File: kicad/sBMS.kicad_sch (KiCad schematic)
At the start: 6 parts, among them J1 SWD, J2 CAN, J3 Conn_01x01_Socket, J4 Conn_01x01_Socket, J5 Conn_01x01_Socket, J6 Conn_01x01_Socket

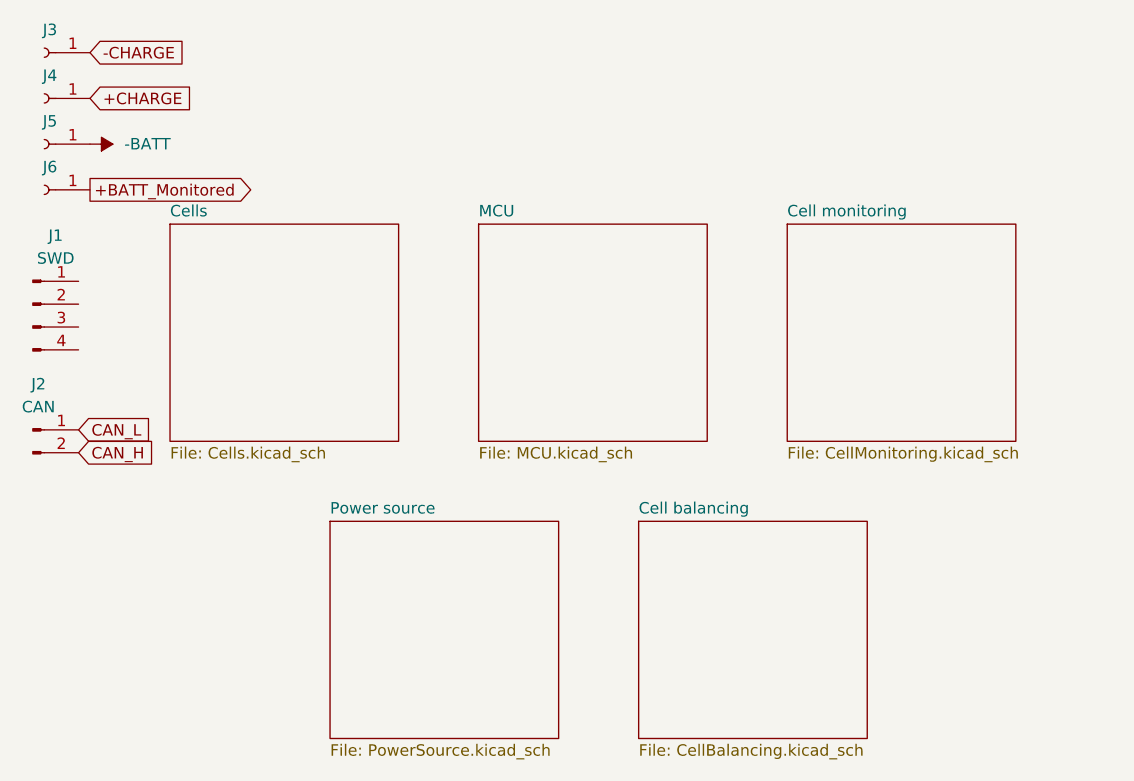
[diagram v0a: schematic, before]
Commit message: fixed cell layout, started making balancing circuitry
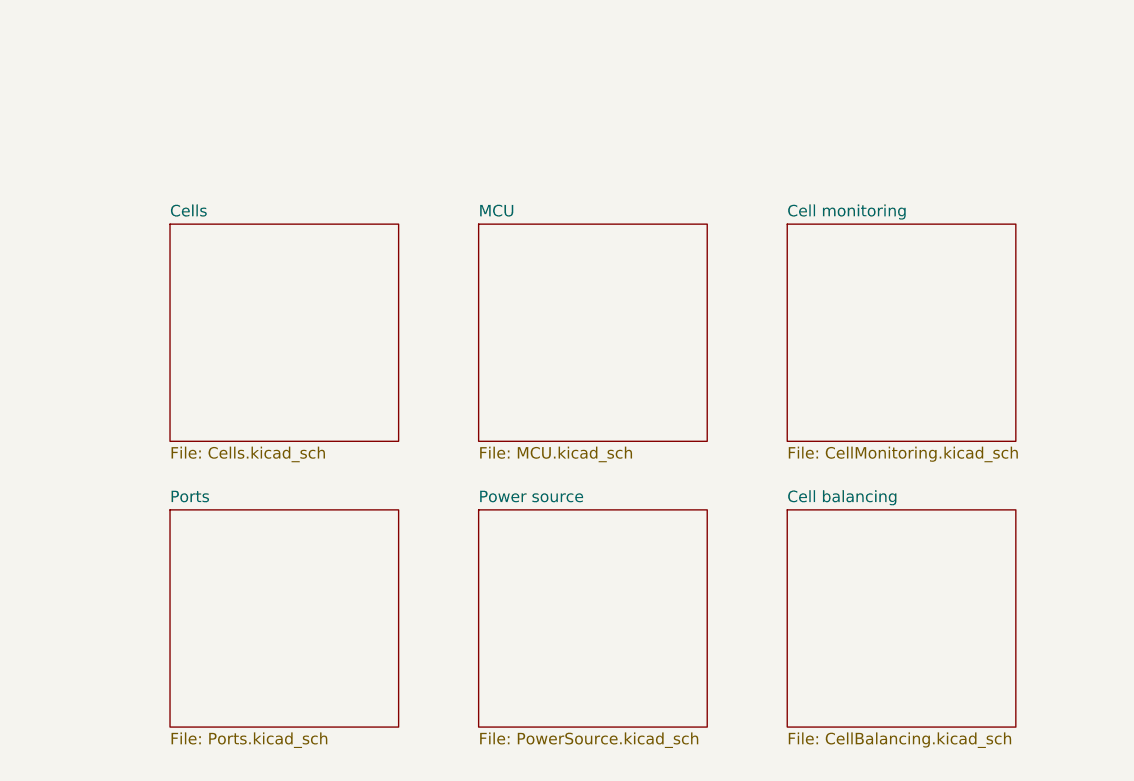
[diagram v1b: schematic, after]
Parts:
- removed J1: SWD, symbol Connector:Conn_01x04_Male
- removed J2: CAN, symbol Connector:Conn_01x02_Male
- removed J3, J4, J5, J6: Conn_01x01_Socket, symbol Connector:Conn_01x01_Socket
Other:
- added sheet Ports (Ports.kicad_sch)
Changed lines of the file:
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@@
     (date "2023-08-20")
-  )
-  (global_label "+BATT_Monitored" (shape output) (at 22.86 34.29 0) (fields_autoplaced)
-    (effects (font (size 1.27 1.27)) (justify left))
-    (property "Intersheetrefs" "${INTERSHEET_REFS}" (at 41.9317 34.29 0)
-      (effects (font (size 1.27 1.27)) (justify left) hide)
-    )
-  )
-  (global_label "CAN_L" (shape input) (at 21.59 60.96 0) (fields_autoplaced)
-    (effects (font (size 1.27 1.27)) (justify left))
-    (property "Intersheetrefs" "${INTERSHEET_REFS}" (at 29.6879 60.8806 0)
-      (effects (font (size 1.27 1.27)) (justify left) hide)
-    )
-  )
-  (global_label "-CHARGE" (shape input) (at 22.86 19.05 0) (fields_autoplaced)
-    (effects (font (size 1.27 1.27)) (justify left))
-    (property "Intersheetrefs" "${INTERSHEET_REFS}" (at 34.7957 19.05 0)
-      (effects (font (size 1.27 1.27)) (justify left) hide)
-    )
-  )
-  (global_label "+CHARGE" (shape input) (at 22.86 24.13 0) (fields_autoplaced)
-    (effects (font (size 1.27 1.27)) (justify left))
-    (property "Intersheetrefs" "${INTERSHEET_REFS}" (at 34.7957 24.13 0)
-      (effects (font (size 1.27 1.27)) (justify left) hide)
-    )
-  )
-  (global_label "CAN_H" (shape input) (at 21.59 63.5 0) (fields_autoplaced)
-    (effects (font (size 1.27 1.27)) (justify left))
-    (property "Intersheetrefs" "${INTERSHEET_REFS}" (at 29.9902 63.4206 0)
-      (effects (font (size 1.27 1.27)) (justify left) hide)
-    )
-  )
-  (symbol (lib_id "Connector:Conn_01x04_Male") (at 16.51 46.99 0) (unit 1)
-    (in_bom yes) (on_board yes) (dnp no)
-    (property "Reference" "J1" (at 19.05 39.37 0)
-      (effects (font (size 1.27 1.27)))
-    )
-    (property "Value" "SWD" (at 19.05 41.91 0)
-      (effects (font (size 1.27 1.27)))
-    )
-    (property "Footprint" "" (at 16.51 46.99 0)
-      (effects (font (size 1.27 1.27)) hide)
-    )
-    (property "Datasheet" "~" (at 16.51 46.99 0)
-      (effects (font (size 1.27 1.27)) hide)
-    )
-    (pin "1")
-    (pin "2")
-    (pin "3")
-    (pin "4")
-    (instances
-      (project "SmartBMS"
-        (path "/7f25f26f-13d1-483f-a85d-b3abae309e30"
-          (reference "J1") (unit 1)
-        )
-      )
-    )
-  )
-  (symbol (lib_id "Connector:Conn_01x01_Socket") (at 17.78 19.05 180) (unit 1)
-    (in_bom yes) (on_board yes) (dnp no) (fields_autoplaced)
-    (property "Reference" "J3" (at 18.415 16.51 0)
-      (effects (font (size 1.27 1.27)))
-    )
-    (property "Value" "Conn_01x01_Socket" (at 18.415 16.51 0)
-      (effects (font (size 1.27 1.27)) hide)
-    )
-    (property "Footprint" "" (at 17.78 19.05 0)
-      (effects (font (size 1.27 1.27)) hide)
-    )
-    (property "Datasheet" "~" (at 17.78 19.05 0)
-      (effects (font (size 1.27 1.27)) hide)
-    )
-    (pin "1")
-    (instances
-      (project "SmartBMS"
-        (path "/7f25f26f-13d1-483f-a85d-b3abae309e30"
-          (reference "J3") (unit 1)
-        )
-      )
-    )
-  )
-  (symbol (lib_id "Connector:Conn_01x02_Male") (at 16.51 60.96 0) (unit 1)
-    (in_bom yes) (on_board yes) (dnp no)
-    (property "Reference" "J2" (at 17.145 55.88 0)
-      (effects (font (size 1.27 1.27)))
-    )
-    (property "Value" "CAN" (at 17.145 58.42 0)
-      (effects (font (size 1.27 1.27)))
-    )
-    (property "Footprint" "" (at 16.51 60.96 0)
-      (effects (font (size 1.27 1.27)) hide)
-    )
-    (property "Datasheet" "~" (at 16.51 60.96 0)
-      (effects (font (size 1.27 1.27)) hide)
-    )
-    (pin "1")
-    (pin "2")
-    (instances
-      (project "SmartBMS"
-        (path "/7f25f26f-13d1-483f-a85d-b3abae309e30"
-          (reference "J2") (unit 1)
-        )
-      )
-    )
-  )
-  (symbol (lib_id "Connector:Conn_01x01_Socket") (at 17.78 29.21 180) (unit 1)
-    (in_bom yes) (on_board yes) (dnp no) (fields_autoplaced)
-    (property "Reference" "J5" (at 18.415 26.67 0)
-      (effects (font (size 1.27 1.27)))
-    )
-    (property "Value" "Conn_01x01_Socket" (at 18.415 26.67 0)
-      (effects (font (size 1.27 1.27)) hide)
-    )
-    (property "Footprint" "" (at 17.78 29.21 0)
-      (effects (font (size 1.27 1.27)) hide)
-    )
-    (property "Datasheet" "~" (at 17.78 29.21 0)
-      (effects (font (size 1.27 1.27)) hide)
-    )
-    (pin "1")
-    (instances
-      (project "SmartBMS"
-        (path "/7f25f26f-13d1-483f-a85d-b3abae309e30"
-          (reference "J5") (unit 1)
-        )
-      )
-    )
-  )
-  (symbol (lib_id "Connector:Conn_01x01_Socket") (at 17.78 34.29 180) (unit 1)
-    (in_bom yes) (on_board yes) (dnp no) (fields_autoplaced)
-    (property "Reference" "J6" (at 18.415 31.75 0)
-      (effects (font (size 1.27 1.27)))
-    )
-    (property "Value" "Conn_01x01_Socket" (at 18.415 31.75 0)
-      (effects (font (size 1.27 1.27)) hide)
-    )
-    (property "Footprint" "" (at 17.78 34.29 0)
-      (effects (font (size 1.27 1.27)) hide)
-    )
-    (property "Datasheet" "~" (at 17.78 34.29 0)
-      (effects (font (size 1.27 1.27)) hide)
-    )
-    (pin "1")
-    (instances
-      (project "SmartBMS"
-        (path "/7f25f26f-13d1-483f-a85d-b3abae309e30"
-          (reference "J6") (unit 1)
-        )
-      )
-    )
-  )
-  (symbol (lib_id "power:-BATT") (at 22.86 29.21 270) (unit 1)
-    (in_bom yes) (on_board yes) (dnp no) (fields_autoplaced)
-    (property "Reference" "#PWR08" (at 19.05 29.21 0)
-      (effects (font (size 1.27 1.27)) hide)
-    )
-    (property "Value" "-BATT" (at 26.67 29.21 90)
-      (effects (font (size 1.27 1.27)) (justify left))
-    )
-    (property "Footprint" "" (at 22.86 29.21 0)
-      (effects (font (size 1.27 1.27)) hide)
-    )
-    (property "Datasheet" "" (at 22.86 29.21 0)
-      (effects (font (size 1.27 1.27)) hide)
-    )
-    (pin "1")
-    (instances
-      (project "SmartBMS"
-        (path "/7f25f26f-13d1-483f-a85d-b3abae309e30"
-          (reference "#PWR08") (unit 1)
-        )
-      )
-    )
-  )
-  (symbol (lib_id "Connector:Conn_01x01_Socket") (at 17.78 24.13 180) (unit 1)
-    (in_bom yes) (on_board yes) (dnp no) (fields_autoplaced)
-    (property "Reference" "J4" (at 18.415 21.59 0)
-      (effects (font (size 1.27 1.27)))
-    )
-    (property "Value" "Conn_01x01_Socket" (at 18.415 21.59 0)
-      (effects (font (size 1.27 1.27)) hide)
-    )
-    (property "Footprint" "" (at 17.78 24.13 0)
-      (effects (font (size 1.27 1.27)) hide)
-    )
-    (property "Datasheet" "~" (at 17.78 24.13 0)
-      (effects (font (size 1.27 1.27)) hide)
-    )
-    (pin "1")
-    (instances
-      (project "SmartBMS"
-        (path "/7f25f26f-13d1-483f-a85d-b3abae309e30"
-          (reference "J4") (unit 1)
-        )
-      )
-    )
   )
   (sheet (at 100.33 38.1) (size 25.4 24.13) (fields_autoplaced)
@@
     )
     (instances
-      (project "SmartBMS"
-        (path "/7f25f26f-13d1-483f-a85d-b3abae309e30" (page "4"))
+      (project "sBMS"
+        (path "/7f25f26f-13d1-483f-a85d-b3abae309e30" (page "5"))
       )
     )
   )
-  (sheet (at 49.53 71.12) (size 25.4 24.13) (fields_autoplaced)
+  (sheet (at 31.75 69.85) (size 25.4 24.13) (fields_autoplaced)
     (stroke (width 0.1524) (type solid))
     (fill (color 0 0 0 0.0000))
-    (property "Sheetname" "Power source" (at 49.53 70.4084 0)
+    (property "Sheetname" "Ports" (at 31.75 69.1384 0)
       (effects (font (size 1.27 1.27)) (justify left bottom))
     )
-    (property "Sheetfile" "PowerSource.kicad_sch" (at 49.53 95.8346 0)
+    (property "Sheetfile" "Ports.kicad_sch" (at 31.75 94.5646 0)
       (effects (font (size 1.27 1.27)) (justify left top))
     )
     (instances
-      (project "SmartBMS"
-        (path "/7f25f26f-13d1-483f-a85d-b3abae309e30" (page "6"))
+      (project "sBMS"
+        (path "/7f25f26f-13d1-483f-a85d-b3abae309e30" (page "2"))
+      )
+    )
+  )
+  (sheet (at 66.04 69.85) (size 25.4 24.13) (fields_autoplaced)
+    (stroke (width 0.1524) (type solid))
+    (fill (color 0 0 0 0.0000))
+    (property "Sheetname" "Power source" (at 66.04 69.1384 0)
+      (effects (font (size 1.27 1.27)) (justify left bottom))
+    )
+    (property "Sheetfile" "PowerSource.kicad_sch" (at 66.04 94.5646 0)
+      (effects (font (size 1.27 1.27)) (justify left top))
+    )
+    (instances
+      (project "sBMS"
+        (path "/7f25f26f-13d1-483f-a85d-b3abae309e30" (page "7"))
       )
     )
@@
     )
     (instances
-      (project "SmartBMS"
-        (path "/7f25f26f-13d1-483f-a85d-b3abae309e30" (page "2"))
+      (project "sBMS"
+        (path "/7f25f26f-13d1-483f-a85d-b3abae309e30" (page "3"))
       )
     )
   )
-  (sheet (at 83.82 71.12) (size 25.4 24.13) (fields_autoplaced)
+  (sheet (at 100.33 69.85) (size 25.4 24.13) (fields_autoplaced)
     (stroke (width 0.1524) (type solid))
     (fill (color 0 0 0 0.0000))
-    (property "Sheetname" "Cell balancing" (at 83.82 70.4084 0)
+    (property "Sheetname" "Cell balancing" (at 100.33 69.1384 0)
       (effects (font (size 1.27 1.27)) (justify left bottom))
     )
-    (property "Sheetfile" "CellBalancing.kicad_sch" (at 83.82 95.8346 0)
+    (property "Sheetfile" "CellBalancing.kicad_sch" (at 100.33 94.5646 0)
       (effects (font (size 1.27 1.27)) (justify left top))
     )
     (instances
-      (project "SmartBMS"
-        (path "/7f25f26f-13d1-483f-a85d-b3abae309e30" (page "5"))
+      (project "sBMS"
+        (path "/7f25f26f-13d1-483f-a85d-b3abae309e30" (page "6"))
       )
     )
@@
     )
     (instances
-      (project "SmartBMS"
-        (path "/7f25f26f-13d1-483f-a85d-b3abae309e30" (page "3"))
+      (project "sBMS"
+        (path "/7f25f26f-13d1-483f-a85d-b3abae309e30" (page "4"))
       )
     )

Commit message: made full cell balancing up to 36S
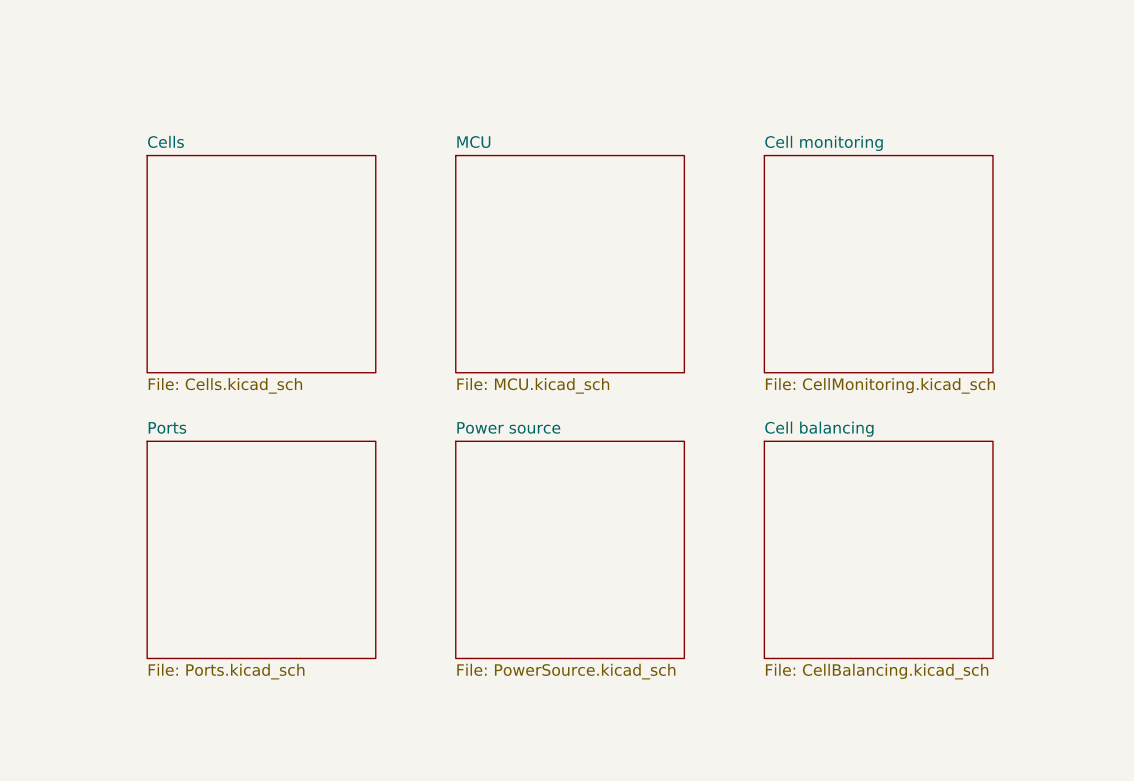
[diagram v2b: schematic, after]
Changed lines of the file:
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@@
     (date "2023-08-20")
   )
-  (sheet (at 100.33 38.1) (size 25.4 24.13) (fields_autoplaced)
+  (sheet (at 97.79 30.48) (size 25.4 24.13) (fields_autoplaced)
     (stroke (width 0.1524) (type solid))
     (fill (color 0 0 0 0.0000))
-    (property "Sheetname" "Cell monitoring" (at 100.33 37.3884 0)
+    (property "Sheetname" "Cell monitoring" (at 97.79 29.7684 0)
       (effects (font (size 1.27 1.27)) (justify left bottom))
     )
-    (property "Sheetfile" "CellMonitoring.kicad_sch" (at 100.33 62.8146 0)
+    (property "Sheetfile" "CellMonitoring.kicad_sch" (at 97.79 55.1946 0)
       (effects (font (size 1.27 1.27)) (justify left top))
     )
@@
     )
   )
-  (sheet (at 31.75 69.85) (size 25.4 24.13) (fields_autoplaced)
+  (sheet (at 29.21 62.23) (size 25.4 24.13) (fields_autoplaced)
     (stroke (width 0.1524) (type solid))
     (fill (color 0 0 0 0.0000))
-    (property "Sheetname" "Ports" (at 31.75 69.1384 0)
+    (property "Sheetname" "Ports" (at 29.21 61.5184 0)
       (effects (font (size 1.27 1.27)) (justify left bottom))
     )
-    (property "Sheetfile" "Ports.kicad_sch" (at 31.75 94.5646 0)
+    (property "Sheetfile" "Ports.kicad_sch" (at 29.21 86.9446 0)
       (effects (font (size 1.27 1.27)) (justify left top))
     )
@@
     )
   )
-  (sheet (at 66.04 69.85) (size 25.4 24.13) (fields_autoplaced)
+  (sheet (at 63.5 62.23) (size 25.4 24.13) (fields_autoplaced)
     (stroke (width 0.1524) (type solid))
     (fill (color 0 0 0 0.0000))
-    (property "Sheetname" "Power source" (at 66.04 69.1384 0)
+    (property "Sheetname" "Power source" (at 63.5 61.5184 0)
       (effects (font (size 1.27 1.27)) (justify left bottom))
     )
-    (property "Sheetfile" "PowerSource.kicad_sch" (at 66.04 94.5646 0)
+    (property "Sheetfile" "PowerSource.kicad_sch" (at 63.5 86.9446 0)
       (effects (font (size 1.27 1.27)) (justify left top))
     )
@@
     )
   )
-  (sheet (at 31.75 38.1) (size 25.4 24.13) (fields_autoplaced)
+  (sheet (at 29.21 30.48) (size 25.4 24.13) (fields_autoplaced)
     (stroke (width 0.1524) (type solid))
     (fill (color 0 0 0 0.0000))
-    (property "Sheetname" "Cells" (at 31.75 37.3884 0)
+    (property "Sheetname" "Cells" (at 29.21 29.7684 0)
       (effects (font (size 1.27 1.27)) (justify left bottom))
     )
-    (property "Sheetfile" "Cells.kicad_sch" (at 31.75 62.8146 0)
+    (property "Sheetfile" "Cells.kicad_sch" (at 29.21 55.1946 0)
       (effects (font (size 1.27 1.27)) (justify left top))
     )
@@
     )
   )
-  (sheet (at 100.33 69.85) (size 25.4 24.13) (fields_autoplaced)
+  (sheet (at 97.79 62.23) (size 25.4 24.13) (fields_autoplaced)
     (stroke (width 0.1524) (type solid))
     (fill (color 0 0 0 0.0000))
-    (property "Sheetname" "Cell balancing" (at 100.33 69.1384 0)
+    (property "Sheetname" "Cell balancing" (at 97.79 61.5184 0)
       (effects (font (size 1.27 1.27)) (justify left bottom))
     )
-    (property "Sheetfile" "CellBalancing.kicad_sch" (at 100.33 94.5646 0)
+    (property "Sheetfile" "CellBalancing.kicad_sch" (at 97.79 86.9446 0)
       (effects (font (size 1.27 1.27)) (justify left top))
     )
@@
     )
   )
-  (sheet (at 66.04 38.1) (size 25.4 24.13) (fields_autoplaced)
+  (sheet (at 63.5 30.48) (size 25.4 24.13) (fields_autoplaced)
     (stroke (width 0.1524) (type solid))
     (fill (color 0 0 0 0.0000))
-    (property "Sheetname" "MCU" (at 66.04 37.3884 0)
+    (property "Sheetname" "MCU" (at 63.5 29.7684 0)
       (effects (font (size 1.27 1.27)) (justify left bottom))
     )
-    (property "Sheetfile" "MCU.kicad_sch" (at 66.04 62.8146 0)
+    (property "Sheetfile" "MCU.kicad_sch" (at 63.5 55.1946 0)
       (effects (font (size 1.27 1.27)) (justify left top))
     )

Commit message: Added firmware boilerplate
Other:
- sheet Power source renamed Power management
- sheet Power management: file PowerSource.kicad_sch -> PowerManagement.kicad_sch
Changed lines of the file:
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@@
     (stroke (width 0.1524) (type solid))
     (fill (color 0 0 0 0.0000))
-    (property "Sheetname" "Power source" (at 63.5 61.5184 0)
+    (property "Sheetname" "Power management" (at 63.5 61.5184 0)
       (effects (font (size 1.27 1.27)) (justify left bottom))
     )
-    (property "Sheetfile" "PowerSource.kicad_sch" (at 63.5 86.9446 0)
+    (property "Sheetfile" "PowerManagement.kicad_sch" (at 63.5 86.9446 0)
       (effects (font (size 1.27 1.27)) (justify left top))
     )
